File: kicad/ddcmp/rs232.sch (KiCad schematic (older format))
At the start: 15 parts, among them J5 DTE, J6 DCE, J7 Bulkhead, U3 MAX3222, U4 MAX3222

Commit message: Schematic and PCB modeling tweaks.
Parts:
- C1, C10, C2, C3, C4, C5, C6, C7, C8, C9: Digikey 399-14010-1-ND​ -> (none); Digikey part (none) -> 399-14010-1-ND; Mfg Kemet -> (none); Mfg part C315C104M5U5TA7301 -> (none); Vendor (none) -> Kemet; Vendor part (none) -> C315C104M5U5TA7301
- J5: Digikey part (none) -> L717SDB25P1ACH4F-ND; Vendor (none) -> Amphenol ICC; Vendor part (none) -> L717SDB25P1ACH4F
- J6: Digikey part (none) -> L77SDB25S1ACH3R-ND; Vendor (none) -> Amphenol ICC; Vendor part (none) -> L77SDB25S1ACH3R
- J7: Digikey part (none) -> 609-1779-ND; Vendor (none) -> Amphenol ICC; Vendor part (none) -> 75869-107LF
- U3, U4: Digikey part (none) -> MAX3222ECPN+-ND; Mfg Maxim -> (none); Mfg part MAX3222ECPN -> (none); Vendor (none) -> Maxim; Vendor part (none) -> MAX3222ECPN
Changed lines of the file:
@@
 $Descr A4 11693 8268
 encoding utf-8
-Sheet 4 4
+Sheet 3 4
 Title "DDCMP Framer"
 Date "2021-05-17"
@@
 F 1 "MAX3222" H 7600 3790 50  0000 C CNN
 F 2 "ddcmp_parts:DIP-18_W7.62mm" H 7650 1450 50  0001 L CNN
-F 3 "" H 7600 2600 50  0001 C CNN
-F 4 "Maxim" H 7600 2500 50  0001 C CNN "Mfg"
-F 5 "MAX3222ECPN" H 7600 2500 50  0001 C CNN "Mfg part"
+F 3 "https://datasheets.maximintegrated.com/en/ds/MAX3222E-MAX3246E.pdf" H 7600 2600 50  0001 C CNN
+F 4 "MAX3222ECPN+-ND" H 0   0   50  0001 C CNN "Digikey part"
+F 5 "Maxim" H 0   0   50  0001 C CNN "Vendor"
+F 6 "MAX3222ECPN" H 0   0   50  0001 C CNN "Vendor part"
 	1    7600 2500
 	1    0    0    -1
@@
 F 1 "MAX3222" H 3700 3790 50  0000 C CNN
 F 2 "ddcmp_parts:DIP-18_W7.62mm" H 3750 1450 50  0001 L CNN
-F 3 "" H 3700 2600 50  0001 C CNN
-F 4 "Maxim" H 3700 2500 50  0001 C CNN "Mfg"
-F 5 "MAX3222ECPN" H 3700 2500 50  0001 C CNN "Mfg part"
+F 3 "https://datasheets.maximintegrated.com/en/ds/MAX3222E-MAX3246E.pdf" H 3700 2600 50  0001 C CNN
+F 4 "MAX3222ECPN+-ND" H 3700 2500 50  0001 C CNN "Digikey part"
+F 5 "Maxim" H 3700 2500 50  0001 C CNN "Vendor"
+F 6 "MAX3222ECPN" H 3700 2500 50  0001 C CNN "Vendor part"
 	1    3700 2500
 	1    0    0    -1
@@
 F 2 "ddcmp_parts:C_Rect_L4.0mm_W2.5mm_P2.54mm" H 2638 1600 50  0001 C CNN
 F 3 "" H 2600 1750 50  0001 C CNN
-F 4 "399-14010-1-ND​" H 2600 1750 50  0001 C CNN "Digikey"
-F 5 "Kemet" H 2600 1750 50  0001 C CNN "Mfg"
-F 6 "C315C104M5U5TA7301" H 2600 1750 50  0001 C CNN "Mfg part"
+F 4 "399-14010-1-ND" H 2600 1750 50  0001 C CNN "Digikey part"
+F 5 "Kemet" H 2600 1750 50  0001 C CNN "Vendor"
+F 6 "C315C104M5U5TA7301" H 2600 1750 50  0001 C CNN "Vendor part"
+F 7 "399-14010-1-ND" H 2600 1750 50  0001 C CNN "Digikey part"
+F 8 "Kemet" H 2600 1750 50  0001 C CNN "Vendor"
+F 9 "C315C104M5U5TA7301" H 2600 1750 50  0001 C CNN "Vendor part"
 	1    2600 1750
 	1    0    0    -1
@@
 F 2 "ddcmp_parts:C_Rect_L4.0mm_W2.5mm_P2.54mm" H 4838 1600 50  0001 C CNN
 F 3 "" H 4800 1750 50  0001 C CNN
-F 4 "399-14010-1-ND​" H 4800 1750 50  0001 C CNN "Digikey"
-F 5 "Kemet" H 4800 1750 50  0001 C CNN "Mfg"
-F 6 "C315C104M5U5TA7301" H 4800 1750 50  0001 C CNN "Mfg part"
+F 4 "399-14010-1-ND" H 4800 1750 50  0001 C CNN "Digikey part"
+F 5 "Kemet" H 4800 1750 50  0001 C CNN "Vendor"
+F 6 "C315C104M5U5TA7301" H 4800 1750 50  0001 C CNN "Vendor part"
+F 7 "399-14010-1-ND" H 4800 1750 50  0001 C CNN "Digikey part"
+F 8 "Kemet" H 4800 1750 50  0001 C CNN "Vendor"
+F 9 "C315C104M5U5TA7301" H 4800 1750 50  0001 C CNN "Vendor part"
 	1    4800 1750
 	1    0    0    -1
@@
 F 2 "ddcmp_parts:C_Rect_L4.0mm_W2.5mm_P2.54mm" H 6438 1600 50  0001 C CNN
 F 3 "" H 6400 1750 50  0001 C CNN
-F 4 "399-14010-1-ND​" H 6400 1750 50  0001 C CNN "Digikey"
-F 5 "Kemet" H 6400 1750 50  0001 C CNN "Mfg"
-F 6 "C315C104M5U5TA7301" H 6400 1750 50  0001 C CNN "Mfg part"
+F 4 "399-14010-1-ND" H 6400 1750 50  0001 C CNN "Digikey part"
+F 5 "Kemet" H 6400 1750 50  0001 C CNN "Vendor"
+F 6 "C315C104M5U5TA7301" H 6400 1750 50  0001 C CNN "Vendor part"
+F 7 "399-14010-1-ND" H 6400 1750 50  0001 C CNN "Digikey part"
+F 8 "Kemet" H 6400 1750 50  0001 C CNN "Vendor"
+F 9 "C315C104M5U5TA7301" H 6400 1750 50  0001 C CNN "Vendor part"
 	1    6400 1750
 	1    0    0    -1
@@
 F 2 "ddcmp_parts:C_Rect_L4.0mm_W2.5mm_P2.54mm" H 8738 1600 50  0001 C CNN
 F 3 "" H 8700 1750 50  0001 C CNN
-F 4 "399-14010-1-ND​" H 8700 1750 50  0001 C CNN "Digikey"
-F 5 "Kemet" H 8700 1750 50  0001 C CNN "Mfg"
-F 6 "C315C104M5U5TA7301" H 8700 1750 50  0001 C CNN "Mfg part"
+F 4 "399-14010-1-ND" H 8700 1750 50  0001 C CNN "Digikey part"
+F 5 "Kemet" H 8700 1750 50  0001 C CNN "Vendor"
+F 6 "C315C104M5U5TA7301" H 8700 1750 50  0001 C CNN "Vendor part"
+F 7 "399-14010-1-ND" H 8700 1750 50  0001 C CNN "Digikey part"
+F 8 "Kemet" H 8700 1750 50  0001 C CNN "Vendor"
+F 9 "C315C104M5U5TA7301" H 8700 1750 50  0001 C CNN "Vendor part"
 	1    8700 1750
 	1    0    0    -1
@@
 F 2 "ddcmp_parts:C_Rect_L4.0mm_W2.5mm_P2.54mm" H 2388 1000 50  0001 C CNN
 F 3 "" H 2350 1150 50  0001 C CNN
-F 4 "399-14010-1-ND​" H 2350 1150 50  0001 C CNN "Digikey"
-F 5 "Kemet" H 2350 1150 50  0001 C CNN "Mfg"
-F 6 "C315C104M5U5TA7301" H 2350 1150 50  0001 C CNN "Mfg part"
+F 4 "399-14010-1-ND" H 2350 1150 50  0001 C CNN "Digikey part"
+F 5 "Kemet" H 2350 1150 50  0001 C CNN "Vendor"
+F 6 "C315C104M5U5TA7301" H 2350 1150 50  0001 C CNN "Vendor part"
+F 7 "399-14010-1-ND" H 2350 1150 50  0001 C CNN "Digikey part"
+F 8 "Kemet" H 2350 1150 50  0001 C CNN "Vendor"
+F 9 "C315C104M5U5TA7301" H 2350 1150 50  0001 C CNN "Vendor part"
 	1    2350 1150
 	1    0    0    -1
@@
 F 2 "ddcmp_parts:C_Rect_L4.0mm_W2.5mm_P2.54mm" H 6188 1000 50  0001 C CNN
 F 3 "" H 6150 1150 50  0001 C CNN
-F 4 "399-14010-1-ND​" H 6150 1150 50  0001 C CNN "Digikey"
-F 5 "Kemet" H 6150 1150 50  0001 C CNN "Mfg"
-F 6 "C315C104M5U5TA7301" H 6150 1150 50  0001 C CNN "Mfg part"
+F 4 "399-14010-1-ND" H 6150 1150 50  0001 C CNN "Digikey part"
+F 5 "Kemet" H 6150 1150 50  0001 C CNN "Vendor"
+F 6 "C315C104M5U5TA7301" H 6150 1150 50  0001 C CNN "Vendor part"
+F 7 "399-14010-1-ND" H 6150 1150 50  0001 C CNN "Digikey part"
+F 8 "Kemet" H 6150 1150 50  0001 C CNN "Vendor"
+F 9 "C315C104M5U5TA7301" H 6150 1150 50  0001 C CNN "Vendor part"
 	1    6150 1150
 	1    0    0    -1
@@
 F 2 "ddcmp_parts:C_Rect_L4.0mm_W2.5mm_P2.54mm" H 5688 2450 50  0001 C CNN
 F 3 "" H 5650 2600 50  0001 C CNN
-F 4 "399-14010-1-ND​" H 5650 2600 50  0001 C CNN "Digikey"
-F 5 "Kemet" H 5650 2600 50  0001 C CNN "Mfg"
-F 6 "C315C104M5U5TA7301" H 5650 2600 50  0001 C CNN "Mfg part"
+F 4 "399-14010-1-ND" H 5650 2600 50  0001 C CNN "Digikey part"
+F 5 "Kemet" H 5650 2600 50  0001 C CNN "Vendor"
+F 6 "C315C104M5U5TA7301" H 5650 2600 50  0001 C CNN "Vendor part"
+F 7 "399-14010-1-ND" H 5650 2600 50  0001 C CNN "Digikey part"
+F 8 "Kemet" H 5650 2600 50  0001 C CNN "Vendor"
+F 9 "C315C104M5U5TA7301" H 5650 2600 50  0001 C CNN "Vendor part"
 	1    5650 2600
 	1    0    0    -1
@@
 F 2 "ddcmp_parts:C_Rect_L4.0mm_W2.5mm_P2.54mm" H 5288 2450 50  0001 C CNN
 F 3 "" H 5250 2600 50  0001 C CNN
-F 4 "399-14010-1-ND​" H 5250 2600 50  0001 C CNN "Digikey"
-F 5 "Kemet" H 5250 2600 50  0001 C CNN "Mfg"
-F 6 "C315C104M5U5TA7301" H 5250 2600 50  0001 C CNN "Mfg part"
+F 4 "399-14010-1-ND" H 5250 2600 50  0001 C CNN "Digikey part"
+F 5 "Kemet" H 5250 2600 50  0001 C CNN "Vendor"
+F 6 "C315C104M5U5TA7301" H 5250 2600 50  0001 C CNN "Vendor part"
+F 7 "399-14010-1-ND" H 5250 2600 50  0001 C CNN "Digikey part"
+F 8 "Kemet" H 5250 2600 50  0001 C CNN "Vendor"
+F 9 "C315C104M5U5TA7301" H 5250 2600 50  0001 C CNN "Vendor part"
 	1    5250 2600
 	1    0    0    -1
@@
 F 2 "ddcmp_parts:C_Rect_L4.0mm_W2.5mm_P2.54mm" H 9138 2450 50  0001 C CNN
 F 3 "" H 9100 2600 50  0001 C CNN
-F 4 "399-14010-1-ND​" H 9100 2600 50  0001 C CNN "Digikey"
-F 5 "Kemet" H 9100 2600 50  0001 C CNN "Mfg"
-F 6 "C315C104M5U5TA7301" H 9100 2600 50  0001 C CNN "Mfg part"
+F 4 "399-14010-1-ND" H 9100 2600 50  0001 C CNN "Digikey part"
+F 5 "Kemet" H 9100 2600 50  0001 C CNN "Vendor"
+F 6 "C315C104M5U5TA7301" H 9100 2600 50  0001 C CNN "Vendor part"
+F 7 "399-14010-1-ND" H 9100 2600 50  0001 C CNN "Digikey part"
+F 8 "Kemet" H 9100 2600 50  0001 C CNN "Vendor"
+F 9 "C315C104M5U5TA7301" H 9100 2600 50  0001 C CNN "Vendor part"
 	1    9100 2600
 	1    0    0    -1
@@
 F 2 "ddcmp_parts:C_Rect_L4.0mm_W2.5mm_P2.54mm" H 9738 2450 50  0001 C CNN
 F 3 "" H 9700 2600 50  0001 C CNN
-F 4 "399-14010-1-ND​" H 9700 2600 50  0001 C CNN "Digikey"
-F 5 "Kemet" H 9700 2600 50  0001 C CNN "Mfg"
-F 6 "C315C104M5U5TA7301" H 9700 2600 50  0001 C CNN "Mfg part"
+F 4 "399-14010-1-ND" H 9700 2600 50  0001 C CNN "Digikey part"
+F 5 "Kemet" H 9700 2600 50  0001 C CNN "Vendor"
+F 6 "C315C104M5U5TA7301" H 9700 2600 50  0001 C CNN "Vendor part"
+F 7 "399-14010-1-ND" H 9700 2600 50  0001 C CNN "Digikey part"
+F 8 "Kemet" H 9700 2600 50  0001 C CNN "Vendor"
+F 9 "C315C104M5U5TA7301" H 9700 2600 50  0001 C CNN "Vendor part"
 	1    9700 2600
 	1    0    0    -1
@@
 F 1 "DTE" H 2580 5561 50  0000 L CNN
 F 2 "ddcmp_parts:Amphenol_DB25M_PCB" H 2400 5650 50  0001 C CNN
-F 3 " ~" H 2400 5650 50  0001 C CNN
+F 3 "https://www.amphenol-icc.com/media/wysiwyg/files/drawing/l717sdxxxp1ach4f.pdf" H 2400 5650 50  0001 C CNN
+F 4 "Amphenol ICC" H 2400 5650 50  0001 C CNN "Vendor"
+F 5 "L717SDB25P1ACH4F-ND" H 2400 5650 50  0001 C CNN "Digikey part"
+F 6 "L717SDB25P1ACH4F" H 2400 5650 50  0001 C CNN "Vendor part"
 	1    2400 5650
 	1    0    0    -1
@@
 F 1 "DCE" H 4580 5561 50  0000 L CNN
 F 2 "ddcmp_parts:Amphenol_DB25F_PCB" H 4400 5650 50  0001 C CNN
-F 3 " ~" H 4400 5650 50  0001 C CNN
+F 3 "https://www.amphenol-icc.com/media/wysiwyg/files/drawing/l77sdxxxs1ach3r.pdf" H 4400 5650 50  0001 C CNN
+F 4 "L77SDB25S1ACH3R-ND" H 4400 5650 50  0001 C CNN "Digikey part"
+F 5 "Amphenol ICC" H 4400 5650 50  0001 C CNN "Vendor"
+F 6 "L77SDB25S1ACH3R" H 4400 5650 50  0001 C CNN "Vendor part"
 	1    4400 5650
 	1    0    0    -1
@@
 F 1 "Bulkhead" H 6050 6676 50  0000 C CNN
 F 2 "ddcmp_parts:Berg_40_pin_DEC_pinout" H 6000 5650 50  0001 C CNN
-F 3 "~" H 6000 5650 50  0001 C CNN
+F 3 "https://cdn.amphenol-icc.com/media/wysiwyg/files/drawing/75869.pdf" H 6000 5650 50  0001 C CNN
+F 4 "609-1779-ND" H 0   0   50  0001 C CNN "Digikey part"
+F 5 "Amphenol ICC" H 0   0   50  0001 C CNN "Vendor"
+F 6 "75869-107LF" H 0   0   50  0001 C CNN "Vendor part"
 	1    6000 5650
 	1    0    0    -1

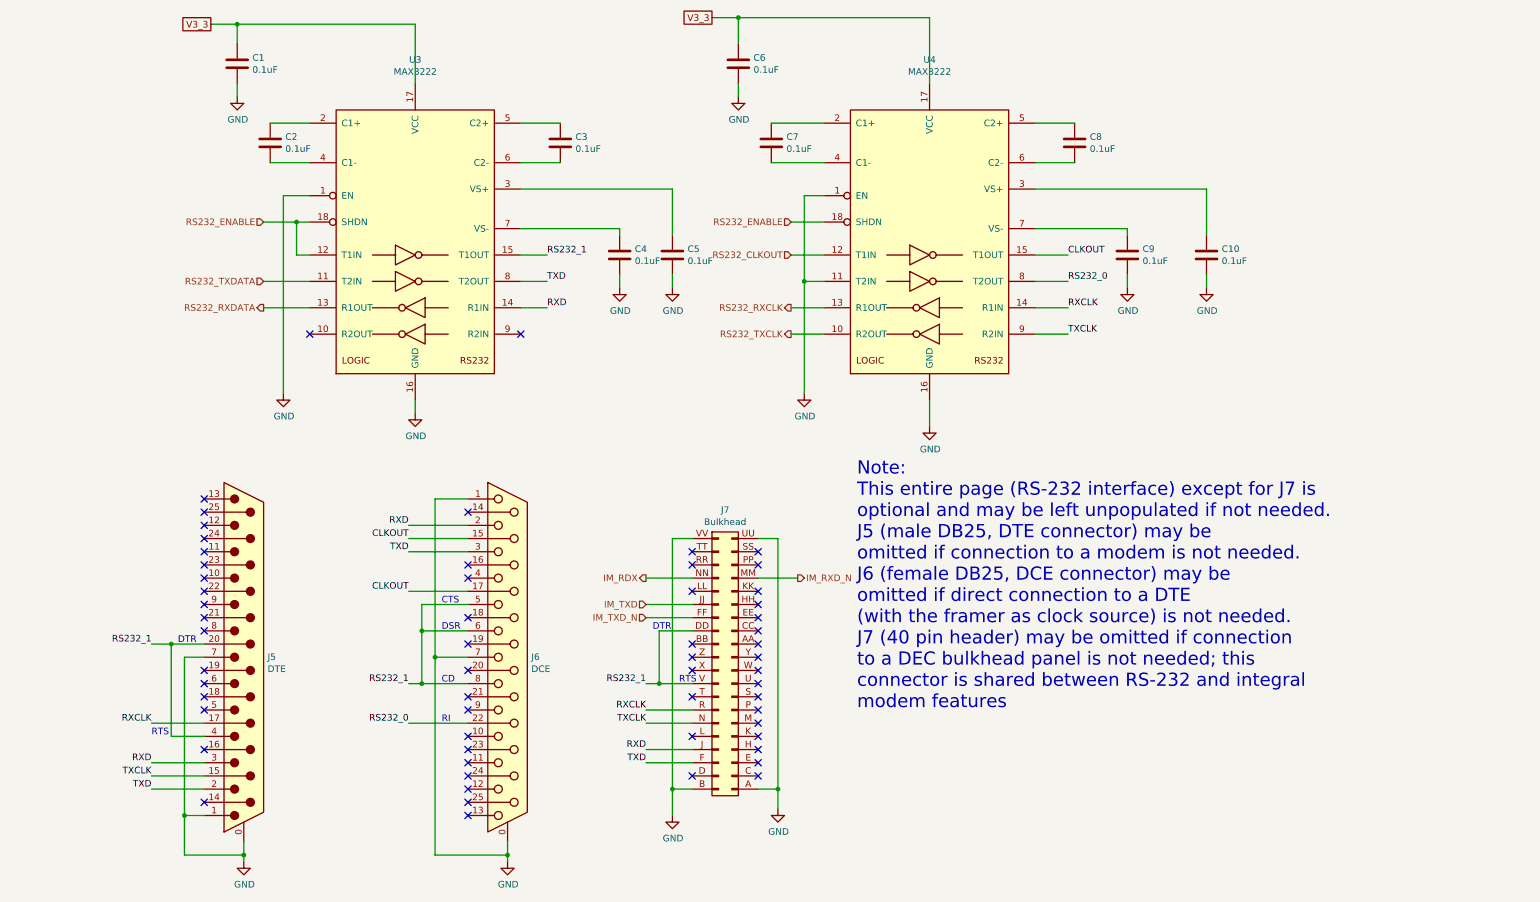
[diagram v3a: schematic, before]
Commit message: Small schematics changes. Rewrite the integral modem receive demodulator state machine.
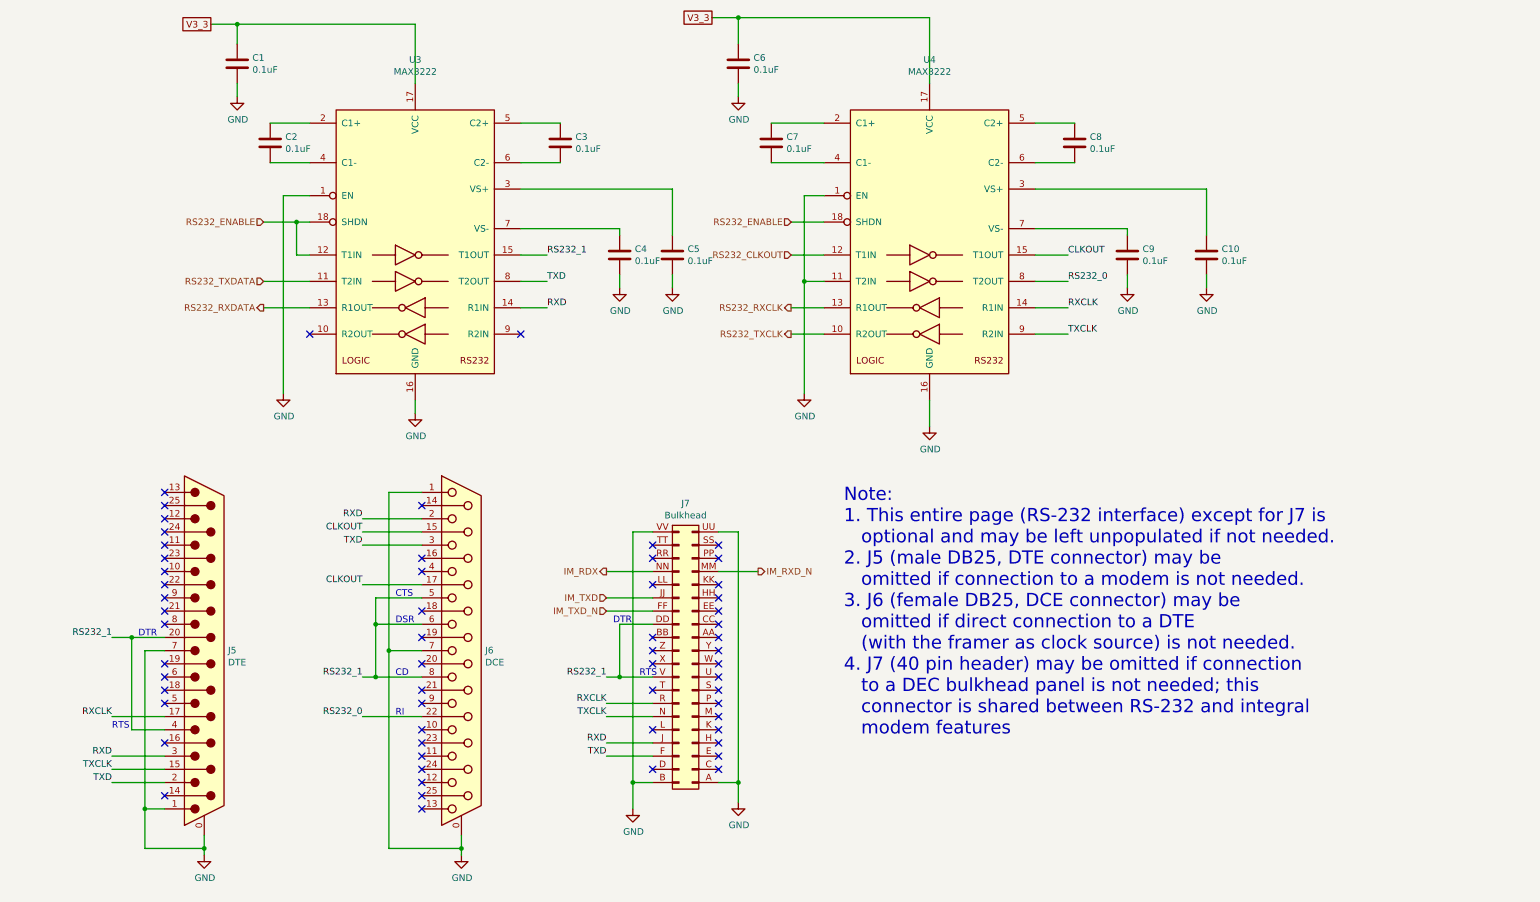
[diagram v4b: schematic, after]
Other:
- note added: "Note:\n1. This entire page (RS-232 interface) except for J7 is \n optional and may be left unpopulated if not needed.\n2. J5 (male DB25, DTE connector) may be \n omitted if connection to a modem is not needed.\n3. J6 (female DB25, DCE connector) may be \n omitted if direct connection to a DTE\n (with the framer as clock source) is not needed.\n4. J7 (40 pin header) may be omitted if connection \n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"
- note removed: "Note:\nThis entire page (RS-232 interface) except for J7 is \noptional and may be left unpopulated if not needed.\nJ5 (male DB25, DTE connector) may be \nomitted if connection to a modem is not needed.\nJ6 (female DB25, DCE connector) may be \nomitted if direct connection to a DTE\n(with the framer as clock source) is not needed.\nJ7 (40 pin header) may be omitted if connection \nto a DEC bulkhea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"
- moved on the sheet: J5, J6, J7

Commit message: Documentation improvements, small schematic fixes. Also firmware improvements, particularly clock rate accuracy.
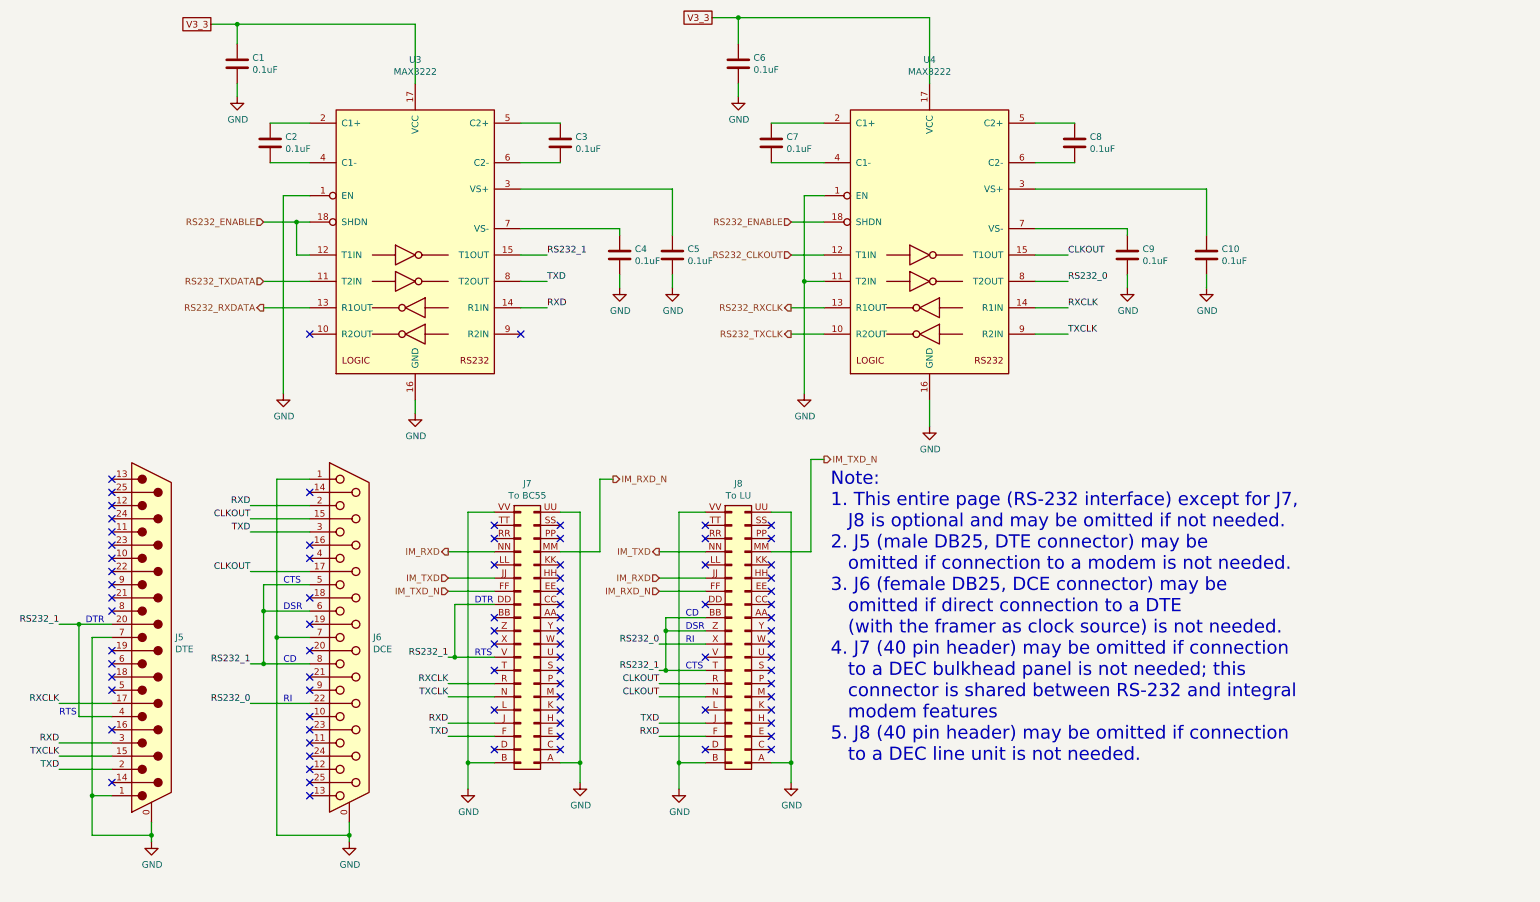
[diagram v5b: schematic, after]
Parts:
- added J8: To LU, ddcmp_parts:Berg_40_pin_DEC_pinout, symbol ddcmp_symbols:Berg_40_pin_DEC_labeling
- J7: value Bulkhead -> To BC55
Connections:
- net CLKOUT: now also J8.N (Pin_29), J8.R (Pin_27)
- net GND: now also J8.A (Pin_40), J8.B (Pin_39), J8.UU (Pin_2), J8.VV (Pin_1)
- net IM_RXD_N: now also J8.FF (Pin_13)
- net IM_TXD: now also J8.NN (Pin_7)
- net IM_TXD_N: now also J8.MM (Pin_8)
- net RS232_0: now also J8.X (Pin_21)
- net RS232_1: now also J8.BB (Pin_17), J8.T (Pin_25), J8.Z (Pin_19)
- net RXD: now also J8.F (Pin_35)
- net TXD: now also J8.J (Pin_33)
- net IM_RDX renamed IM_RXD
- net IM_RXD: now also J8.JJ (Pin_11)
- no-connect marks 60 -> 84
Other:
- note added: "Note:\n1. This entire page (RS-232 interface) except for J7,\n J8 is optional and may be omitted if not needed.\n2. J5 (male DB25, DTE connector) may be \n omitted if connection to a modem is not needed.\n3. J6 (female DB25, DCE connector) may be \n omitted if direct connection to a DTE\n (with the framer as clock source) is not needed.\n4. J7 (40 pin header) may be omitted if connection \n to a 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"
- note removed: "Note:\n1. This entire page (RS-232 interface) except for J7 is \n optional and may be left unpopulated if not needed.\n2. J5 (male DB25, DTE connector) may be \n omitted if connection to a modem is not needed.\n3. J6 (female DB25, DCE connector) may be \n omitted if direct connection to a DTE\n (with the framer as clock source) is not needed.\n4. J7 (40 pin header) may be omitted if connection \n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"
- moved on the sheet: J5, J6, J7
